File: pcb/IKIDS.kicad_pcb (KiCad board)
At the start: 2 copper layers, 142.9 x 95.3 mm, 25 parts, among them U1 Elite-C

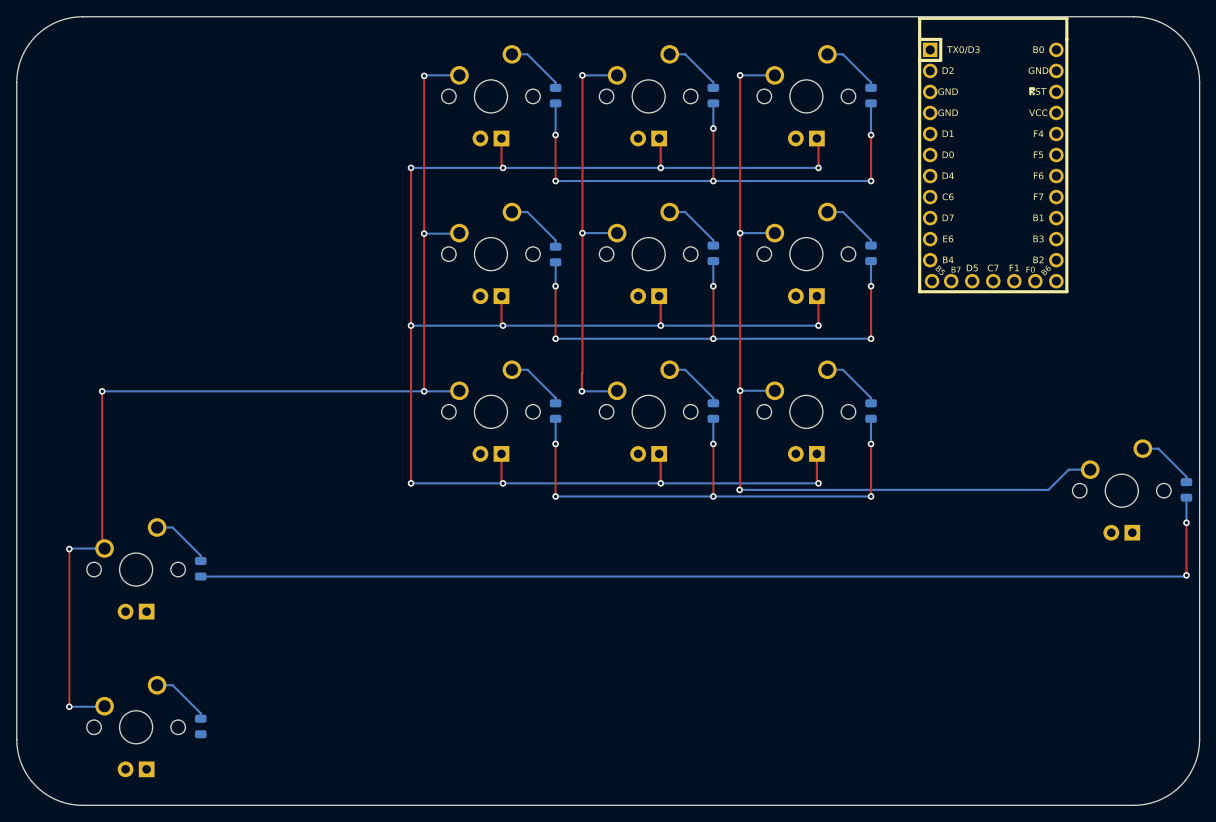
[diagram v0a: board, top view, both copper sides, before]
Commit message: Hooked up main matrix and ground pins for the LED to the MCU.
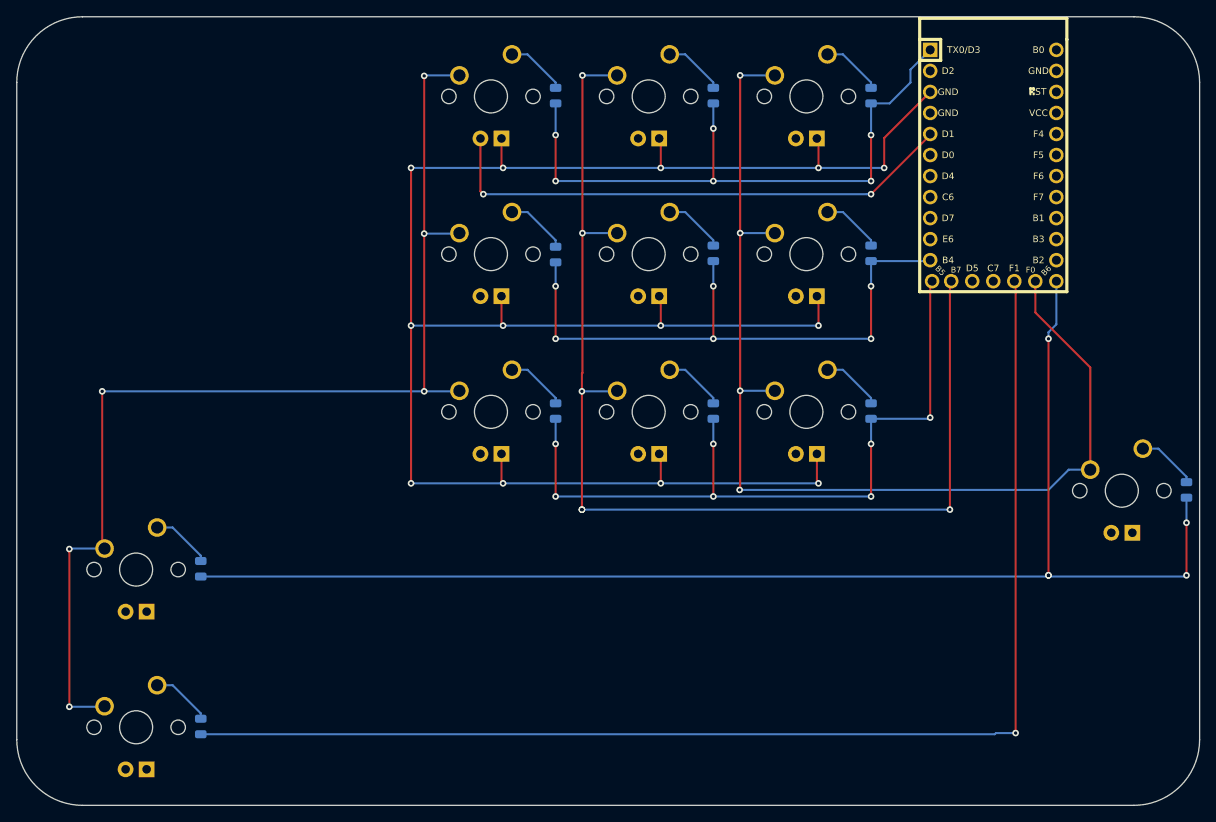
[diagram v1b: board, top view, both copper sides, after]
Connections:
- U1 pad 1: Net-(U1-Pad1) -> row1
- U1 pad 11: col2 -> row2
- U1 pad 12: col3 -> row3
- U1 pad 13: led9 -> row4
- U1 pad 24: led1 -> Net-(U1-Pad24)
- U1 pad 25: Net-(U1-Pad25) -> col2
- U1 pad 28: Net-(U1-Pad28) -> row5
- U1 pad 29: Net-(U1-Pad29) -> col3
- U1 pad 5: row1 -> led1
- U1 pad 6: row2 -> Net-(U1-Pad6)
- U1 pad 7: row3 -> Net-(U1-Pad7)
- U1 pad 8: row4 -> Net-(U1-Pad8)
- U1 pad 9: row5 -> Net-(U1-Pad9)
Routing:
- net row5: track 0.00 -> 153.1 mm, vias 0 -> 1
- net col2: track 50.9 -> 137.2 mm, vias 3 -> 6
- net led1: track 0.00 -> 63.9 mm, vias 0 -> 2
- net row4: track 128.5 -> 164.6 mm, vias 2 -> 5
- net col3: track 106.0 -> 131.5 mm
- net row3: track 66.2 -> 90.0 mm, vias 6 -> 7
- net gnd: track 218.5 -> 237.9 mm, vias 12 -> 13
- net row1: track 66.2 -> 77.0 mm
- net row2: track 66.1 -> 73.3 mm

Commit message: Hooked up top 3 LEDs
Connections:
- U1 pad 19: led3 -> Net-(U1-Pad19)
- U1 pad 20: led2 -> Net-(U1-Pad20)
- U1 pad 6: Net-(U1-Pad6) -> led2
- U1 pad 7: Net-(U1-Pad7) -> led3
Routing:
- net led2: track 0.00 -> 43.4 mm, vias 0 -> 3
- net led3: track 0.00 -> 20.4 mm, vias 0 -> 1
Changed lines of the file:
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@@
     (thickness 1.6)
     (drawings 8)
-    (tracks 228)
+    (tracks 245)
     (zones 0)
     (modules 25)
@@
   (net 42 "Net-(U1-Pad4)")
   (net 43 "Net-(U1-Pad2)")
-  (net 44 "Net-(U1-Pad6)")
-  (net 45 "Net-(U1-Pad7)")
-  (net 46 "Net-(U1-Pad9)")
-  (net 47 "Net-(U1-Pad8)")
-  (net 48 "Net-(U1-Pad24)")
+  (net 44 "Net-(U1-Pad9)")
+  (net 45 "Net-(U1-Pad8)")
+  (net 46 "Net-(U1-Pad24)")
+  (net 47 "Net-(U1-Pad20)")
+  (net 48 "Net-(U1-Pad19)")
   (net_class Default "This is the default net class."
     (clearance 0.2)
@@
     (add_net "Net-(MX2-Pad3)")
     (add_net "Net-(MX2-Pad4)")
+    (add_net "Net-(U1-Pad19)")
     (add_net "Net-(U1-Pad2)")
+    (add_net "Net-(U1-Pad20)")
     (add_net "Net-(U1-Pad21)")
     (add_net "Net-(U1-Pad22)")
@@
     (add_net "Net-(U1-Pad27)")
     (add_net "Net-(U1-Pad4)")
-    (add_net "Net-(U1-Pad6)")
-    (add_net "Net-(U1-Pad7)")
     (add_net "Net-(U1-Pad8)")
     (add_net "Net-(U1-Pad9)")
@@
       (net 32 col3))
     (pad 24 thru_hole circle (at -13.97 -7.62 270) (size 1.7526 1.7526) (drill 1.0922) (layers *.Cu *.SilkS *.Mask)
-      (net 48 "Net-(U1-Pad24)"))
+      (net 46 "Net-(U1-Pad24)"))
     (pad 12 thru_hole circle (at 13.97 7.3914 270) (size 1.7526 1.7526) (drill 1.0922) (layers *.Cu *.SilkS *.Mask)
       (net 10 row3))
@@
       (net 41 "Net-(U1-Pad21)"))
     (pad 20 thru_hole circle (at -3.81 -7.62 270) (size 1.7526 1.7526) (drill 1.0922) (layers *.Cu *.SilkS *.Mask)
-      (net 27 led2))
+      (net 47 "Net-(U1-Pad20)"))
     (pad 19 thru_hole circle (at -1.27 -7.62 270) (size 1.7526 1.7526) (drill 1.0922) (layers *.Cu *.SilkS *.Mask)
-      (net 31 led3))
+      (net 48 "Net-(U1-Pad19)"))
     (pad 18 thru_hole circle (at 1.27 -7.62 270) (size 1.7526 1.7526) (drill 1.0922) (layers *.Cu *.SilkS *.Mask)
       (net 25 led4))
@@
       (net 20 col1))
     (pad 9 thru_hole circle (at 6.35 7.62 270) (size 1.7526 1.7526) (drill 1.0922) (layers *.Cu *.SilkS *.Mask)
-      (net 46 "Net-(U1-Pad9)"))
+      (net 44 "Net-(U1-Pad9)"))
     (pad 8 thru_hole circle (at 3.81 7.62 270) (size 1.7526 1.7526) (drill 1.0922) (layers *.Cu *.SilkS *.Mask)
-      (net 47 "Net-(U1-Pad8)"))
+      (net 45 "Net-(U1-Pad8)"))
     (pad 7 thru_hole circle (at 1.27 7.62 270) (size 1.7526 1.7526) (drill 1.0922) (layers *.Cu *.SilkS *.Mask)
-      (net 45 "Net-(U1-Pad7)"))
+      (net 31 led3))
     (pad 6 thru_hole circle (at -1.27 7.62 270) (size 1.7526 1.7526) (drill 1.0922) (layers *.Cu *.SilkS *.Mask)
-      (net 44 "Net-(U1-Pad6)"))
+      (net 27 led2))
     (pad 5 thru_hole circle (at -3.81 7.62 270) (size 1.7526 1.7526) (drill 1.0922) (layers *.Cu *.SilkS *.Mask)
       (net 24 led1))
@@
   (segment (start 181.76875 73.025) (end 181.76875 72.898) (width 0.25) (layer F.Cu) (net 24))
   (segment (start 174.625 80.16875) (end 181.76875 73.025) (width 0.25) (layer F.Cu) (net 24))
+  (via (at 146.84375 79.375) (size 0.8) (drill 0.4) (layers F.Cu B.Cu) (net 27))
+  (segment (start 146.4945 79.02575) (end 146.84375 79.375) (width 0.25) (layer F.Cu) (net 27))
+  (segment (start 146.4945 73.43775) (end 146.4945 79.02575) (width 0.25) (layer F.Cu) (net 27))
+  (segment (start 181.00675 75.438) (end 181.76875 75.438) (width 0.25) (layer B.Cu) (net 27))
+  (segment (start 180.975 75.40625) (end 181.00675 75.438) (width 0.25) (layer B.Cu) (net 27))
+  (segment (start 146.84375 79.375) (end 177.00625 79.375) (width 0.25) (layer B.Cu) (net 27))
+  (segment (start 177.00625 79.375) (end 177.00625 79.375) (width 0.25) (layer B.Cu) (net 27))
+  (via (at 177.00625 79.375) (size 0.8) (drill 0.4) (layers F.Cu B.Cu) (net 27))
+  (segment (start 177.00625 79.375) (end 177.00625 79.375) (width 0.25) (layer B.Cu) (net 27))
+  (via (at 177.00625 79.375) (size 0.8) (drill 0.4) (layers F.Cu B.Cu) (net 27))
+  (segment (start 177.83175 79.375) (end 181.76875 75.438) (width 0.25) (layer F.Cu) (net 27))
+  (segment (start 177.00625 79.375) (end 177.83175 79.375) (width 0.25) (layer F.Cu) (net 27))
   (segment (start 143.9545 65.81775) (end 139.7635 65.81775) (width 0.25) (layer B.Cu) (net 28))
   (segment (start 139.7635 65.81775) (end 139.7635 65.81775) (width 0.25) (layer B.Cu) (net 28))
@@
   (segment (start 184.15 90.83675) (end 184.30875 90.678) (width 0.25) (layer F.Cu) (net 28))
   (segment (start 184.15 118.26875) (end 184.15 90.83675) (width 0.25) (layer F.Cu) (net 28))
+  (segment (start 165.5445 73.43775) (end 165.5445 77.43825) (width 0.25) (layer F.Cu) (net 31))
+  (via (at 165.89375 77.7875) (size 0.8) (drill 0.4) (layers F.Cu B.Cu) (net 31))
+  (segment (start 165.5445 77.43825) (end 165.89375 77.7875) (width 0.25) (layer F.Cu) (net 31))
+  (segment (start 181.57825 77.7875) (end 181.76875 77.978) (width 0.25) (layer B.Cu) (net 31))
+  (segment (start 165.89375 77.7875) (end 181.57825 77.7875) (width 0.25) (layer B.Cu) (net 31))
   (segment (start 163.0045 65.81775) (end 158.8135 65.81775) (width 0.25) (layer B.Cu) (net 32))
   (via (at 158.8135 65.81775) (size 0.8) (drill 0.4) (layers F.Cu B.Cu) (net 32))

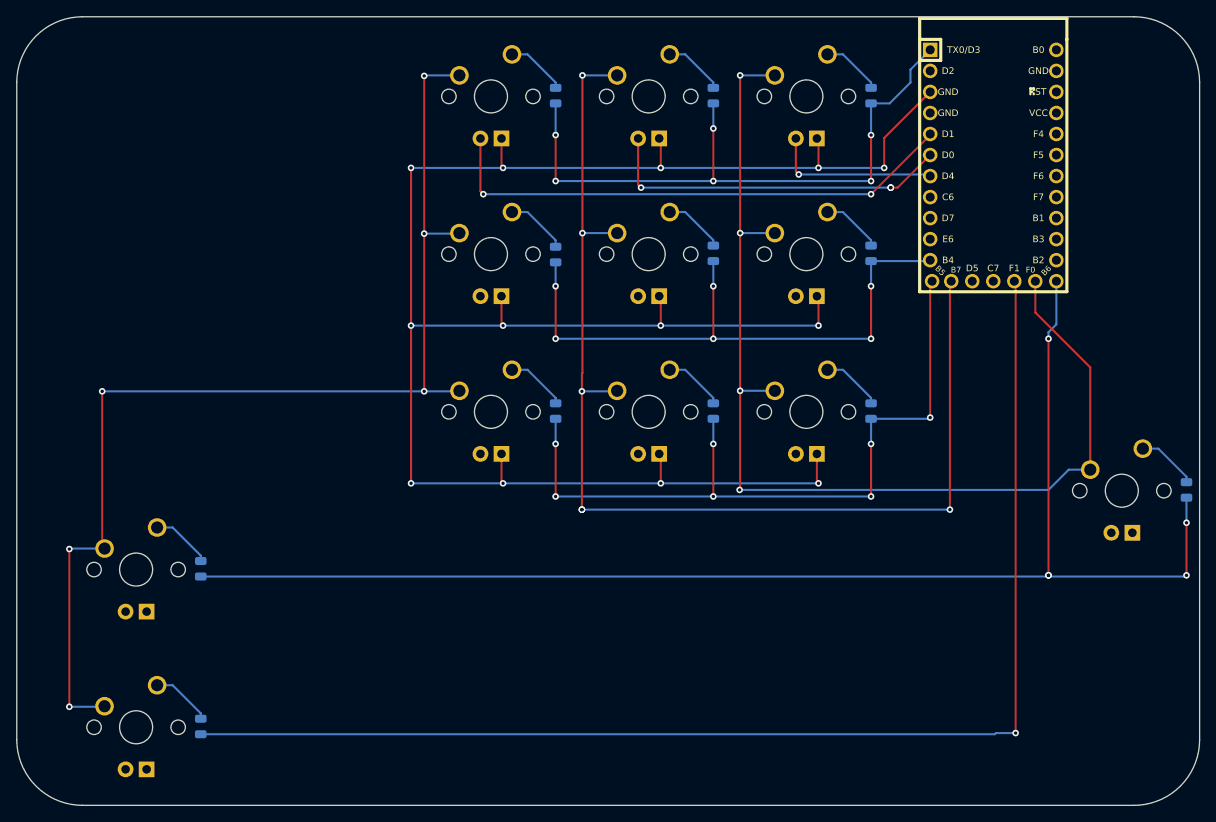
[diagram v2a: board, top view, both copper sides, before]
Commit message: hooked up bottom 3 LEDS
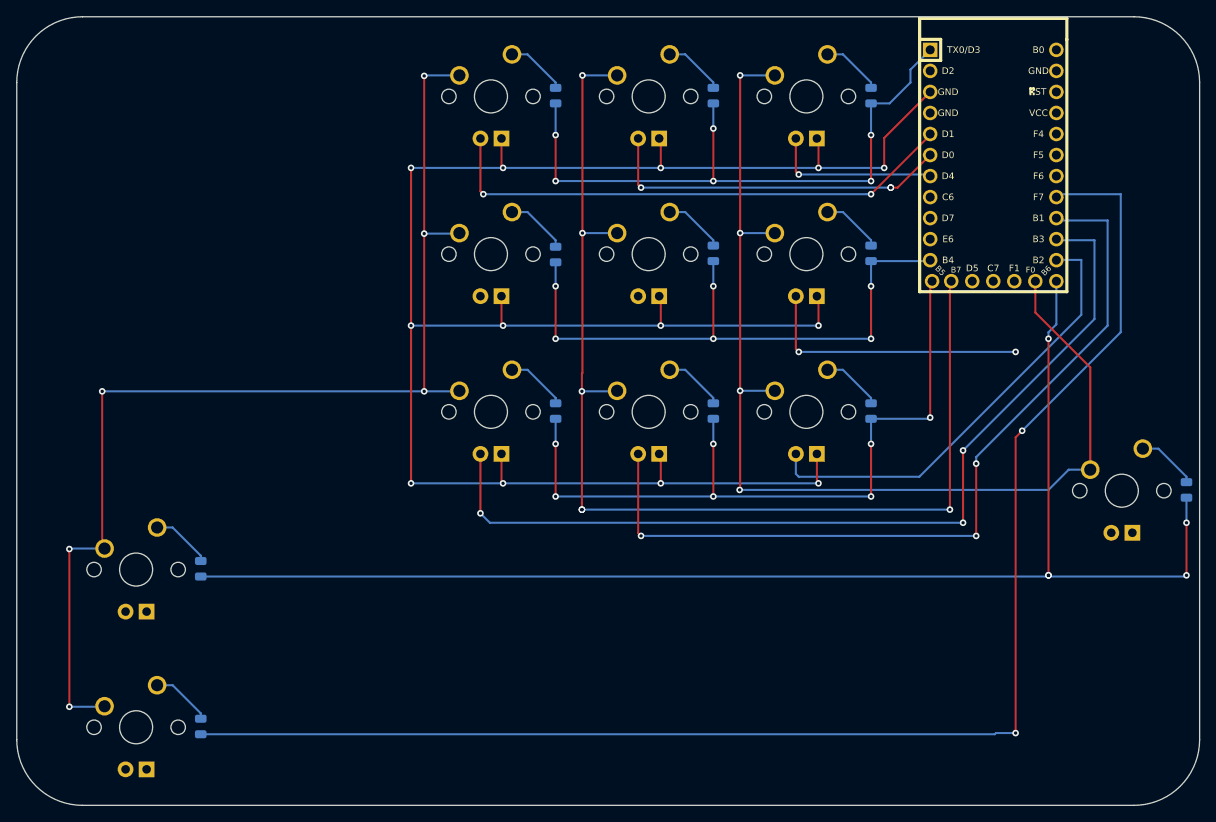
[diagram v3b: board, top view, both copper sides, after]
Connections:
- U1 pad 14: led8 -> led9
- U1 pad 16: led6 -> led8
- U1 pad 17: led5 -> row5
- U1 pad 18: led4 -> Net-(U1-Pad18)
- U1 pad 28: row5 -> Net-(U1-Pad28)
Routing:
- net led7: track 0.00 -> 111.3 mm, vias 0 -> 3
- net led8: track 0.00 -> 101.5 mm, vias 0 -> 3
- net led9: track 0.00 -> 54.8 mm
- net led6: track 0.00 -> 33.1 mm, vias 0 -> 2
- net row5: track 153.1 -> 176.8 mm, vias 1 -> 2

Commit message: Finished PCB and updated Schematics to fit PCB
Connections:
- U1 pad 26: Net-(U1-Pad26) -> led4
- U1 pad 27: Net-(U1-Pad27) -> led5
- U1 pad 28: Net-(U1-Pad28) -> led6
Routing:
- net led4: track 0.00 -> 65.6 mm
- net led5: track 0.00 -> 58.1 mm, vias 0 -> 1
- net led6: track 33.1 -> 41.9 mm
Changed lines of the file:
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@@
     (thickness 1.6)
     (drawings 8)
-    (tracks 287)
+    (tracks 301)
     (zones 0)
     (modules 25)
-    (nets 51)
+    (nets 48)
   )
   (page A4)
@@
   (net 35 "Net-(MX12-Pad4)")
   (net 36 "Net-(MX12-Pad3)")
-  (net 37 "Net-(U1-Pad26)")
-  (net 38 "Net-(U1-Pad27)")
-  (net 39 "Net-(U1-Pad28)")
-  (net 40 "Net-(U1-Pad23)")
-  (net 41 "Net-(U1-Pad22)")
-  (net 42 "Net-(U1-Pad21)")
-  (net 43 "Net-(U1-Pad4)")
-  (net 44 "Net-(U1-Pad2)")
-  (net 45 "Net-(U1-Pad9)")
-  (net 46 "Net-(U1-Pad8)")
-  (net 47 "Net-(U1-Pad24)")
-  (net 48 "Net-(U1-Pad20)")
-  (net 49 "Net-(U1-Pad19)")
-  (net 50 "Net-(U1-Pad18)")
+  (net 37 "Net-(U1-Pad23)")
+  (net 38 "Net-(U1-Pad22)")
+  (net 39 "Net-(U1-Pad21)")
+  (net 40 "Net-(U1-Pad4)")
+  (net 41 "Net-(U1-Pad2)")
+  (net 42 "Net-(U1-Pad9)")
+  (net 43 "Net-(U1-Pad8)")
+  (net 44 "Net-(U1-Pad24)")
+  (net 45 "Net-(U1-Pad20)")
+  (net 46 "Net-(U1-Pad19)")
+  (net 47 "Net-(U1-Pad18)")
   (net_class Default "This is the default net class."
     (clearance 0.2)
@@
     (add_net "Net-(U1-Pad23)")
     (add_net "Net-(U1-Pad24)")
-    (add_net "Net-(U1-Pad26)")
-    (add_net "Net-(U1-Pad27)")
-    (add_net "Net-(U1-Pad28)")
     (add_net "Net-(U1-Pad4)")
     (add_net "Net-(U1-Pad8)")
@@
       (net 28 col2))
     (pad 26 thru_hole circle (at 13.97 2.54 270) (size 1.7526 1.7526) (drill 1.0922) (layers *.Cu *.SilkS *.Mask)
-      (net 37 "Net-(U1-Pad26)"))
+      (net 25 led4))
     (pad 27 thru_hole circle (at 13.97 0 270) (size 1.7526 1.7526) (drill 1.0922) (layers *.Cu *.SilkS *.Mask)
-      (net 38 "Net-(U1-Pad27)"))
+      (net 29 led5))
     (pad 28 thru_hole circle (at 13.97 -2.54 270) (size 1.7526 1.7526) (drill 1.0922) (layers *.Cu *.SilkS *.Mask)
-      (net 39 "Net-(U1-Pad28)"))
+      (net 33 led6))
     (pad 29 thru_hole circle (at 13.97 -5.08 270) (size 1.7526 1.7526) (drill 1.0922) (layers *.Cu *.SilkS *.Mask)
       (net 32 col3))
     (pad 24 thru_hole circle (at -13.97 -7.62 270) (size 1.7526 1.7526) (drill 1.0922) (layers *.Cu *.SilkS *.Mask)
-      (net 47 "Net-(U1-Pad24)"))
+      (net 44 "Net-(U1-Pad24)"))
     (pad 12 thru_hole circle (at 13.97 7.3914 270) (size 1.7526 1.7526) (drill 1.0922) (layers *.Cu *.SilkS *.Mask)
       (net 10 row3))
     (pad 23 thru_hole circle (at -11.43 -7.62 270) (size 1.7526 1.7526) (drill 1.0922) (layers *.Cu *.SilkS *.Mask)
-      (net 40 "Net-(U1-Pad23)"))
+      (net 37 "Net-(U1-Pad23)"))
     (pad 22 thru_hole circle (at -8.89 -7.62 270) (size 1.7526 1.7526) (drill 1.0922) (layers *.Cu *.SilkS *.Mask)
-      (net 41 "Net-(U1-Pad22)"))
+      (net 38 "Net-(U1-Pad22)"))
     (pad 21 thru_hole circle (at -6.35 -7.62 270) (size 1.7526 1.7526) (drill 1.0922) (layers *.Cu *.SilkS *.Mask)
-      (net 42 "Net-(U1-Pad21)"))
+      (net 39 "Net-(U1-Pad21)"))
     (pad 20 thru_hole circle (at -3.81 -7.62 270) (size 1.7526 1.7526) (drill 1.0922) (layers *.Cu *.SilkS *.Mask)
-      (net 48 "Net-(U1-Pad20)"))
+      (net 45 "Net-(U1-Pad20)"))
     (pad 19 thru_hole circle (at -1.27 -7.62 270) (size 1.7526 1.7526) (drill 1.0922) (layers *.Cu *.SilkS *.Mask)
-      (net 49 "Net-(U1-Pad19)"))
+      (net 46 "Net-(U1-Pad19)"))
     (pad 18 thru_hole circle (at 1.27 -7.62 270) (size 1.7526 1.7526) (drill 1.0922) (layers *.Cu *.SilkS *.Mask)
-      (net 50 "Net-(U1-Pad18)"))
+      (net 47 "Net-(U1-Pad18)"))
     (pad 17 thru_hole circle (at 3.81 -7.62 270) (size 1.7526 1.7526) (drill 1.0922) (layers *.Cu *.SilkS *.Mask)
       (net 4 row5))
@@
       (net 20 col1))
     (pad 9 thru_hole circle (at 6.35 7.62 270) (size 1.7526 1.7526) (drill 1.0922) (layers *.Cu *.SilkS *.Mask)
-      (net 45 "Net-(U1-Pad9)"))
+      (net 42 "Net-(U1-Pad9)"))
     (pad 8 thru_hole circle (at 3.81 7.62 270) (size 1.7526 1.7526) (drill 1.0922) (layers *.Cu *.SilkS *.Mask)
-      (net 46 "Net-(U1-Pad8)"))
+      (net 43 "Net-(U1-Pad8)"))
     (pad 7 thru_hole circle (at 1.27 7.62 270) (size 1.7526 1.7526) (drill 1.0922) (layers *.Cu *.SilkS *.Mask)
       (net 31 led3))
@@
       (net 24 led1))
     (pad 4 thru_hole circle (at -6.35 7.62 270) (size 1.7526 1.7526) (drill 1.0922) (layers *.Cu *.SilkS *.Mask)
-      (net 43 "Net-(U1-Pad4)"))
+      (net 40 "Net-(U1-Pad4)"))
     (pad 3 thru_hole circle (at -8.89 7.62 270) (size 1.7526 1.7526) (drill 1.0922) (layers *.Cu *.SilkS *.Mask)
       (net 23 gnd))
     (pad 2 thru_hole circle (at -11.43 7.62 270) (size 1.7526 1.7526) (drill 1.0922) (layers *.Cu *.SilkS *.Mask)
-      (net 44 "Net-(U1-Pad2)"))
+      (net 41 "Net-(U1-Pad2)"))
     (pad 1 thru_hole rect (at -13.97 7.62 270) (size 1.7526 1.7526) (drill 1.0922) (layers *.Cu *.SilkS *.Mask)
       (net 6 row1))
@@
   (segment (start 204.7875 96.8375) (end 204.7875 80.16875) (width 0.25) (layer B.Cu) (net 4))
   (segment (start 192.88125 108.74375) (end 204.7875 96.8375) (width 0.25) (layer B.Cu) (net 4))
-  (segment (start 192.0875 90.83675) (end 191.92875 90.678) (width 0.25) (layer F.Cu) (net 39))
+  (segment (start 192.0875 90.83675) (end 191.92875 90.678) (width 0.25) (layer F.Cu) (net 33))
   (segment (start 131.2545 63.27775) (end 133.12775 63.27775) (width 0.25) (layer B.Cu) (net 5))
   (segment (start 136.525 66.675) (end 136.525 67.325) (width 0.25) (layer B.Cu) (net 5))
@@
   (segment (start 181.76875 73.025) (end 181.76875 72.898) (width 0.25) (layer F.Cu) (net 24))
   (segment (start 174.625 80.16875) (end 181.76875 73.025) (width 0.25) (layer F.Cu) (net 24))
+  (segment (start 127.4445 92.48775) (end 127.4445 94.107) (width 0.25) (layer B.Cu) (net 25))
+  (segment (start 127.4445 94.107) (end 127.79375 94.45625) (width 0.25) (layer B.Cu) (net 25))
+  (segment (start 127.79375 94.45625) (end 187.325 94.45625) (width 0.25) (layer B.Cu) (net 25))
+  (segment (start 187.325 91.15425) (end 186.84875 90.678) (width 0.25) (layer B.Cu) (net 25))
+  (segment (start 187.325 94.45625) (end 187.325 91.15425) (width 0.25) (layer B.Cu) (net 25))
   (segment (start 127.4445 111.53775) (end 127.4445 118.71325) (width 0.25) (layer F.Cu) (net 26))
   (segment (start 127.4445 118.71325) (end 127.4445 118.71325) (width 0.25) (layer F.Cu) (net 26))
@@
   (segment (start 184.15 90.83675) (end 184.30875 90.678) (width 0.25) (layer F.Cu) (net 28))
   (segment (start 184.15 118.26875) (end 184.15 90.83675) (width 0.25) (layer F.Cu) (net 28))
+  (via (at 146.05 99.21875) (size 0.8) (drill 0.4) (layers F.Cu B.Cu) (net 29))
+  (segment (start 146.4945 98.77425) (end 146.05 99.21875) (width 0.25) (layer F.Cu) (net 29))
+  (segment (start 146.4945 92.48775) (end 146.4945 98.77425) (width 0.25) (layer F.Cu) (net 29))
+  (segment (start 146.912499 98.356251) (end 188.981249 98.356251) (width 0.25) (layer B.Cu) (net 29))
+  (segment (start 146.05 99.21875) (end 146.912499 98.356251) (width 0.25) (layer B.Cu) (net 29))
+  (segment (start 189.38875 97.94875) (end 189.38875 90.678) (width 0.25) (layer B.Cu) (net 29))
+  (segment (start 188.981249 98.356251) (end 189.38875 97.94875) (width 0.25) (layer B.Cu) (net 29))
   (segment (start 146.4945 111.53775) (end 146.4945 121.0945) (width 0.25) (layer F.Cu) (net 30))
   (via (at 146.84375 121.44375) (size 0.8) (drill 0.4) (layers F.Cu B.Cu) (net 30))
@@
   (segment (start 165.89375 99.21875) (end 192.0875 99.21875) (width 0.25) (layer B.Cu) (net 33))
   (via (at 192.0875 99.21875) (size 0.8) (drill 0.4) (layers F.Cu B.Cu) (net 33))
+  (segment (start 191.92875 99.06) (end 192.0875 99.21875) (width 0.25) (layer F.Cu) (net 33))
+  (segment (start 191.92875 90.678) (end 191.92875 99.06) (width 0.25) (layer F.Cu) (net 33))
   (segment (start 197.0405 88.10625) (end 197.00875 88.138) (width 0.25) (layer B.Cu) (net 34))
   (segment (start 200.025 88.10625) (end 197.0405 88.10625) (width 0.25) (layer B.Cu) (net 34))
